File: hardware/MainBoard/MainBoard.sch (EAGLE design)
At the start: 26 parts, among them J1 CON-71439-2164, J2 CON-71741-2184-TOP, J3 CON-FTSH-105-01-L-DV-K, J4 CON-ZX62R-B-5P, J5 CON-SMA, J6 CON-SMA, U1 A2F500M3G-FG256, U2 MAX19706-T4877-4, U3 MAX19706-T4877-4, U4 USBLC6-2SC6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

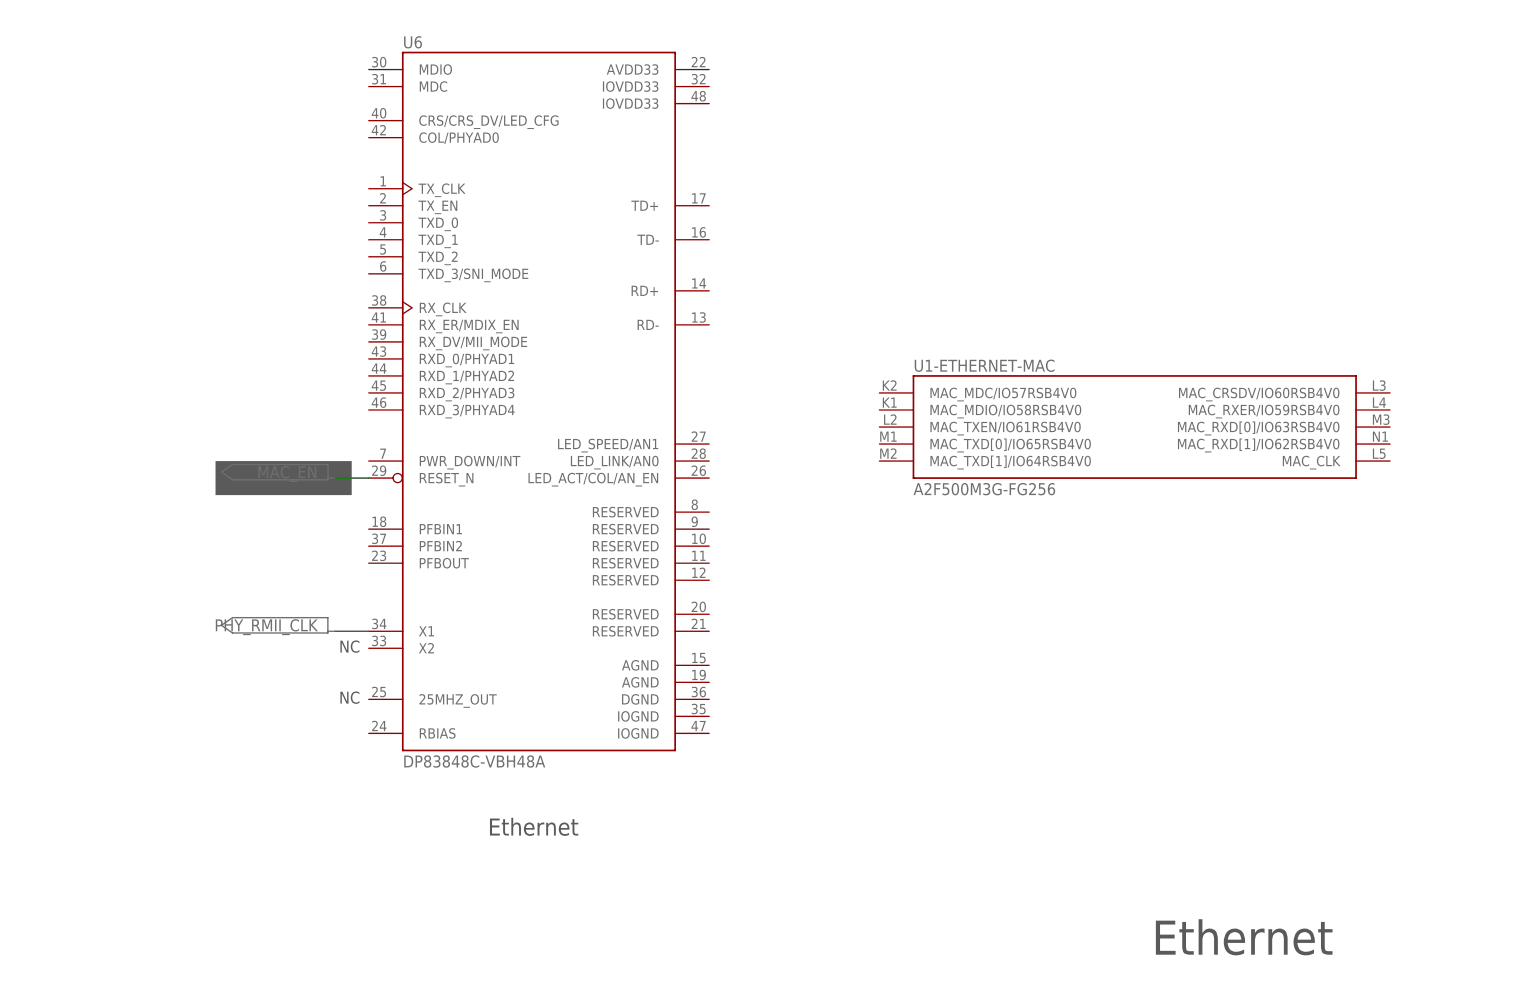
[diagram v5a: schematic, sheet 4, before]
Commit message: Minor updates on schematic (clocking).
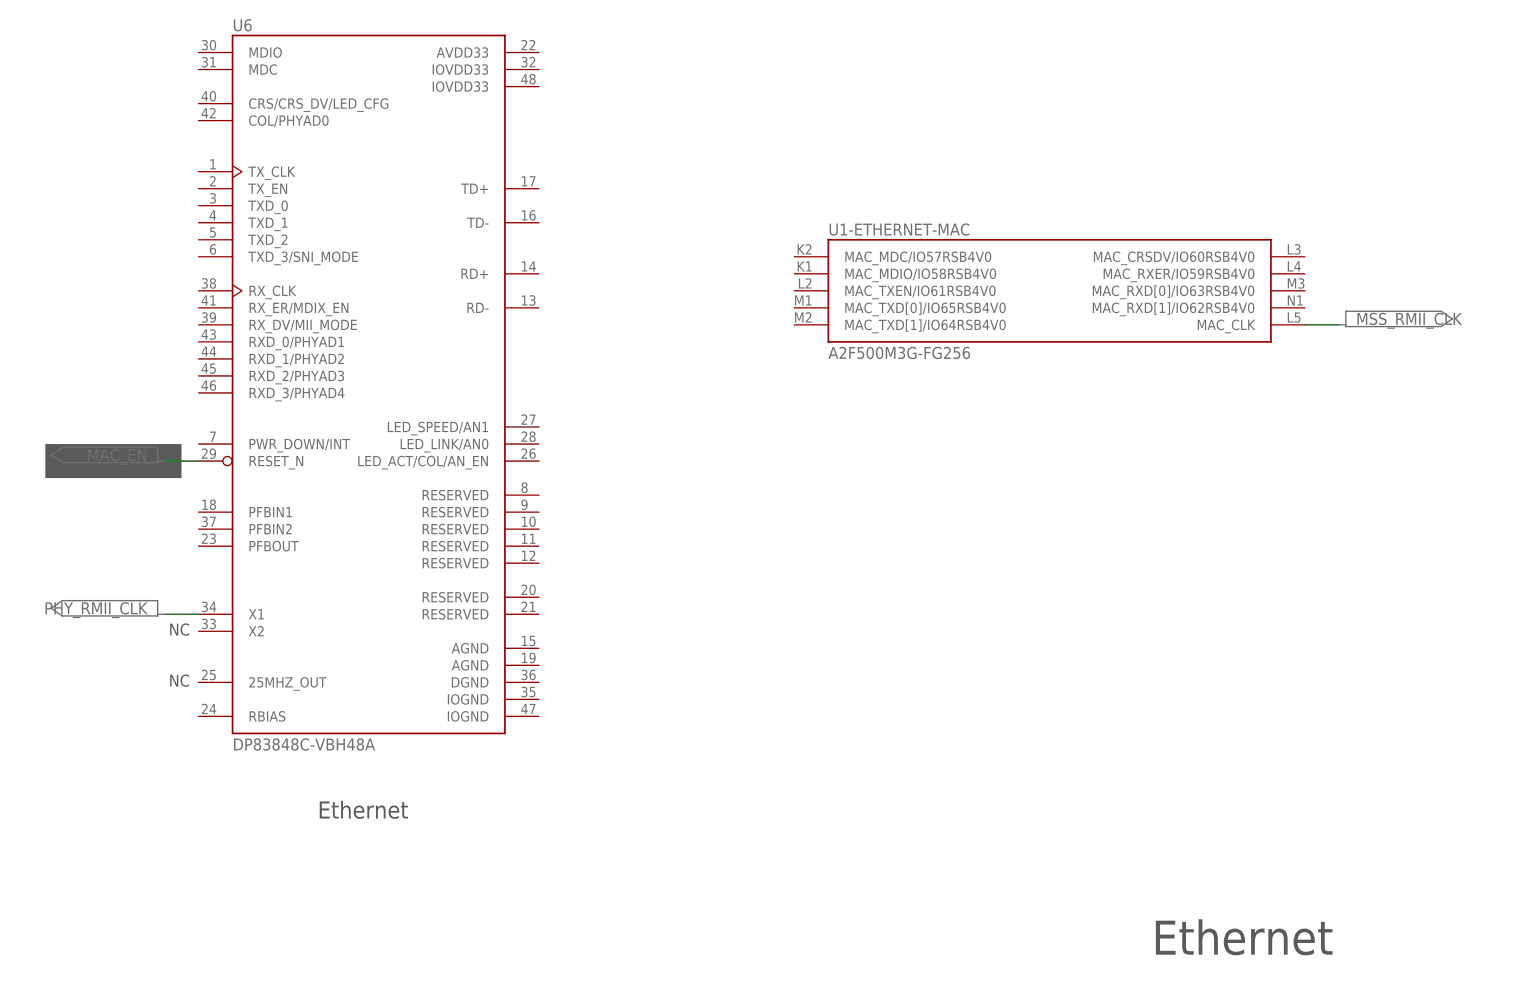
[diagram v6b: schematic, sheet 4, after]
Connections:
- removed net N$8: X1.FO
- new net MAIN_CLK: U1-IOB.GFA2/IO85PDB5V0, X1.FO
- new net USB_CLK: U5.ACBUS5
- net MSS_RMII_CLK: now also U1-ETHERNET-MAC.MAC_CLK
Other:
- note added: "Ethernet oscillator - 50 MHz"
- note added: "Internal oscillators - 20 MHz / 32 kHz"
- note added: "Main oscillator - 20 MHz"
- moved on the sheet: C1, C2, C3, C4, U1-ETHERNET-MAC, U1-EXTERNAL-MEMORY-CONTROLLER, U1-MISC, U6, X2, X3

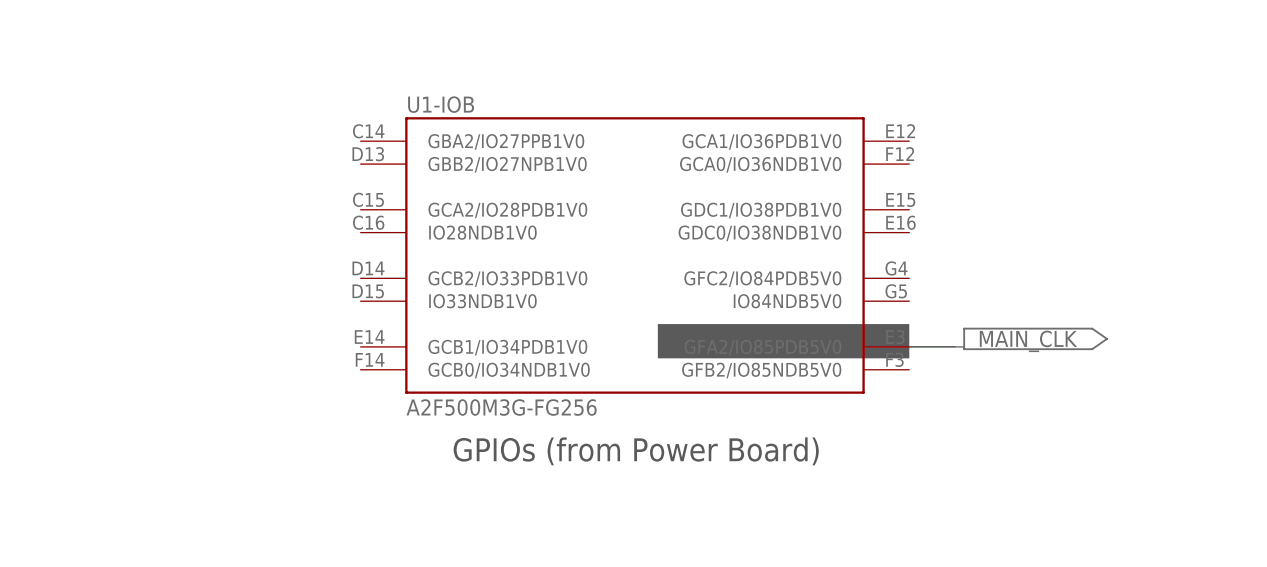
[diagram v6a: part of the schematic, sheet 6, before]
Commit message: Clock signals checked in datasheet and Libero, and added to schematic with the exception of the ADC clocks.
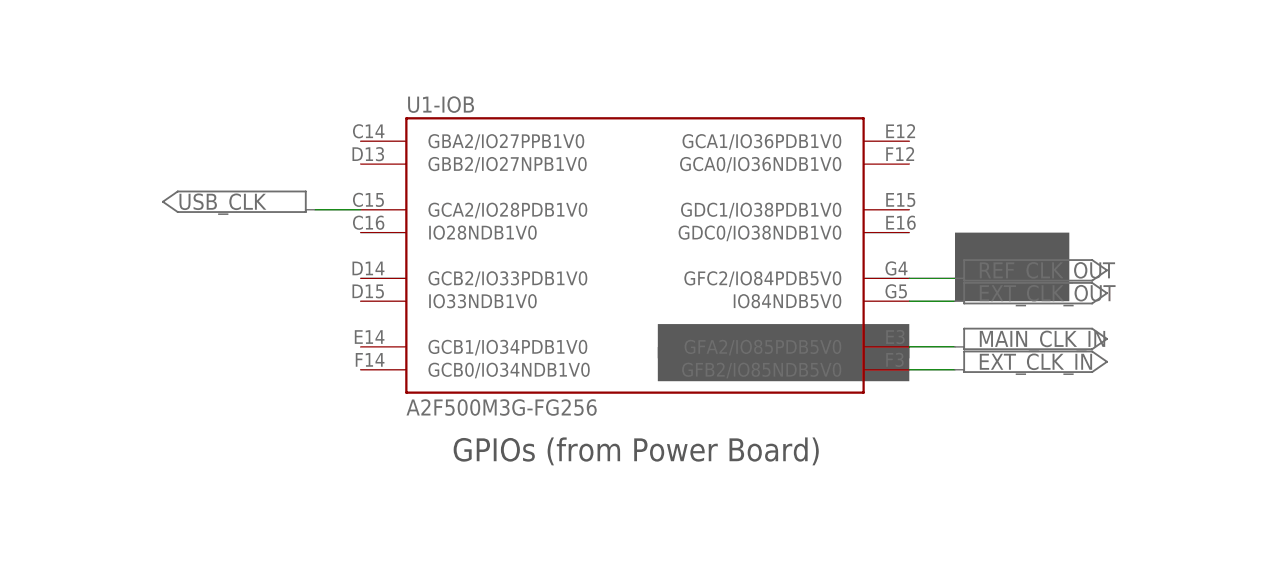
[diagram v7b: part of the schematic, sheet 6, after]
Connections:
- net MAIN_CLK renamed MAIN_CLK_IN
- new net REF_CLK_OUT: U1-IOB.GFC2/IO84PDB5V0
- net EXT_CLK_IN: now also U1-IOB.GFB2/IO85NDB5V0
- net EXT_CLK_OUT: now also U1-IOB.IO84NDB5V0
- net USB_CLK: now also U1-IOB.GCA2/IO28PDB1V0
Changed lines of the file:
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@@
 <part name="PORT54" library="MainBoard" deviceset="PORT7" device=""/>
 <part name="PORT55" library="MainBoard" deviceset="PORT7" device=""/>
+<part name="PORT56" library="MainBoard" deviceset="PORT7" device=""/>
+<part name="PORT57" library="MainBoard" deviceset="PORT7" device=""/>
+<part name="PORT58" library="MainBoard" deviceset="PORT7" device=""/>
+<part name="PORT59" library="MainBoard" deviceset="PORT7" device=""/>
 </parts>
 <sheets>
@@
 </segment>
 </net>
-<net name="MAIN_CLK" class="0">
+<net name="MAIN_CLK_IN" class="0">
 <segment>
 <pinref part="X1" gate="G$1" pin="FO"/>
@@
 <text x="46.355" y="60.325" size="1.778" layer="97">NC</text>
 <rectangle x1="27.94" y1="91.44" x2="48.26" y2="96.52" layer="97"/>
+<text x="46.355" y="136.525" size="1.778" layer="97">NC</text>
+<text x="46.355" y="118.745" size="1.778" layer="97">NC</text>
 </plain>
 <instances>
@@
 <rectangle x1="25.4" y1="152.4" x2="45.72" y2="162.56" layer="97"/>
 <rectangle x1="182.88" y1="64.77" x2="210.82" y2="68.58" layer="97"/>
+<rectangle x1="182.88" y1="62.23" x2="210.82" y2="66.04" layer="97"/>
+<rectangle x1="215.9" y1="71.12" x2="228.6" y2="78.74" layer="97"/>
 </plain>
 <instances>
@@
 <instance part="U1" gate="-IOB" x="180.34" y="76.2"/>
 <instance part="PORT54" gate="G$1" x="231.14" y="66.04"/>
+<instance part="PORT56" gate="G$1" x="231.14" y="63.5"/>
+<instance part="PORT57" gate="G$1" x="129.54" y="81.28" rot="MR0"/>
+<instance part="PORT58" gate="G$1" x="231.14" y="71.12"/>
+<instance part="PORT59" gate="G$1" x="231.14" y="73.66"/>
 </instances>
 <busses>
 </busses>
 <nets>
-<net name="MAIN_CLK" class="0">
+<net name="MAIN_CLK_IN" class="0">
 <segment>
 <pinref part="U1" gate="-IOB" pin="GFA2/IO85PDB5V0"/>
@@
 </segment>
 </net>
+<net name="EXT_CLK_IN" class="0">
+<segment>
+<pinref part="U1" gate="-IOB" pin="GFB2/IO85NDB5V0"/>
+<wire x1="210.82" y1="63.5" x2="215.9" y2="63.5" width="0.1524" layer="91"/>
+<label x="218.44" y="63.5" size="1.778" layer="95"/>
+</segment>
+</net>
+<net name="USB_CLK" class="0">
+<segment>
+<pinref part="U1" gate="-IOB" pin="GCA2/IO28PDB1V0"/>
+<wire x1="149.86" y1="81.28" x2="144.78" y2="81.28" width="0.1524" layer="91"/>
+<label x="129.54" y="81.28" size="1.778" layer="95"/>
+</segment>
+</net>
+<net name="REF_CLK_OUT" class="0">
+<segment>
+<pinref part="U1" gate="-IOB" pin="GFC2/IO84PDB5V0"/>
+<wire x1="210.82" y1="73.66" x2="215.9" y2="73.66" width="0.1524" layer="91"/>
+<label x="218.44" y="73.66" size="1.778" layer="95"/>
+</segment>
+</net>
+<net name="EXT_CLK_OUT" class="0">
+<segment>
+<pinref part="U1" gate="-IOB" pin="IO84NDB5V0"/>
+<wire x1="210.82" y1="71.12" x2="215.9" y2="71.12" width="0.1524" layer="91"/>
+<label x="218.44" y="71.12" size="1.778" layer="95"/>
+</segment>
+</net>
